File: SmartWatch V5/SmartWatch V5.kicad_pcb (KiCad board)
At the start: 4 copper layers, 23.7 x 34.2 mm, 61 parts, among them J1 10118192-0001LF, J10 TestPad, J2 , J8 TestPad, J9 TestPad, Q1 FDN340P, Q2 MMBT3904, Q3 MMBT3904, Q4 FDN028N20, Q5 FDN028N20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

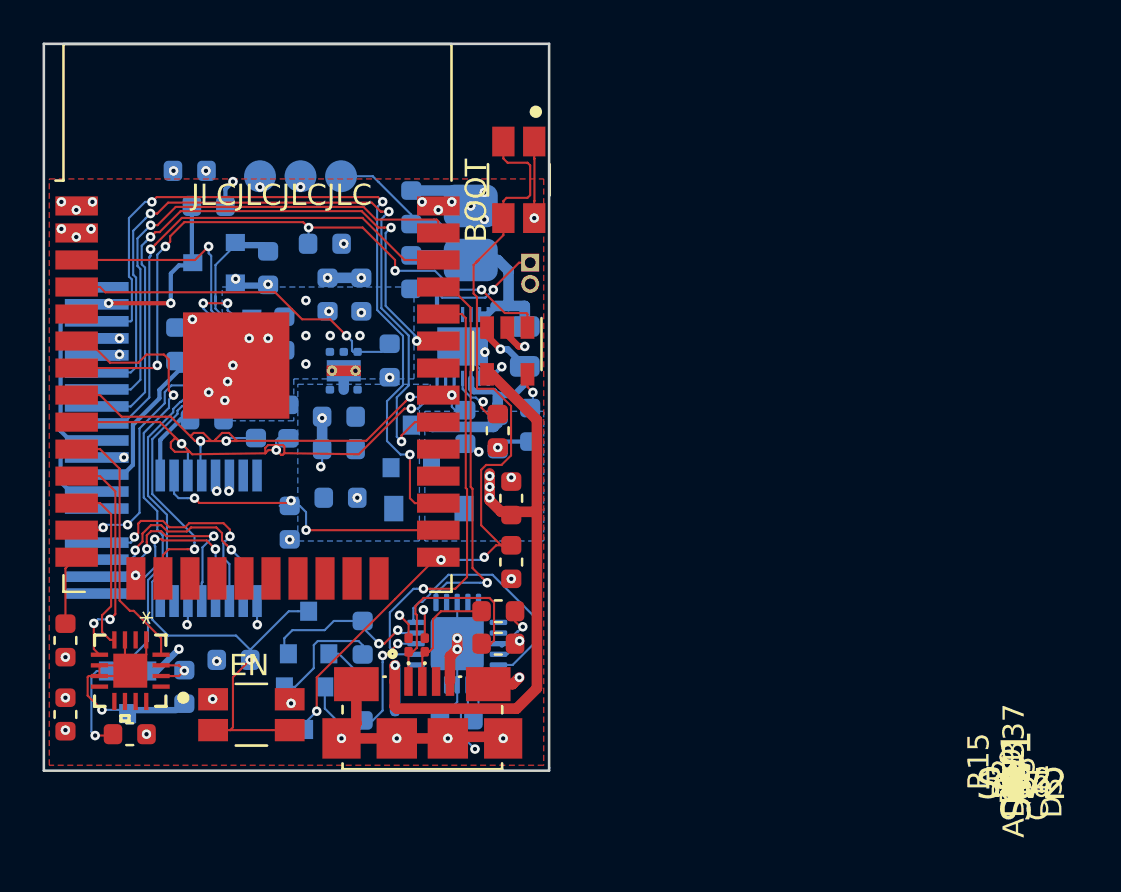
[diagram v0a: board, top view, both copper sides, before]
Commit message: Changed V5 schematic to remove enable mosfet from accelerometer
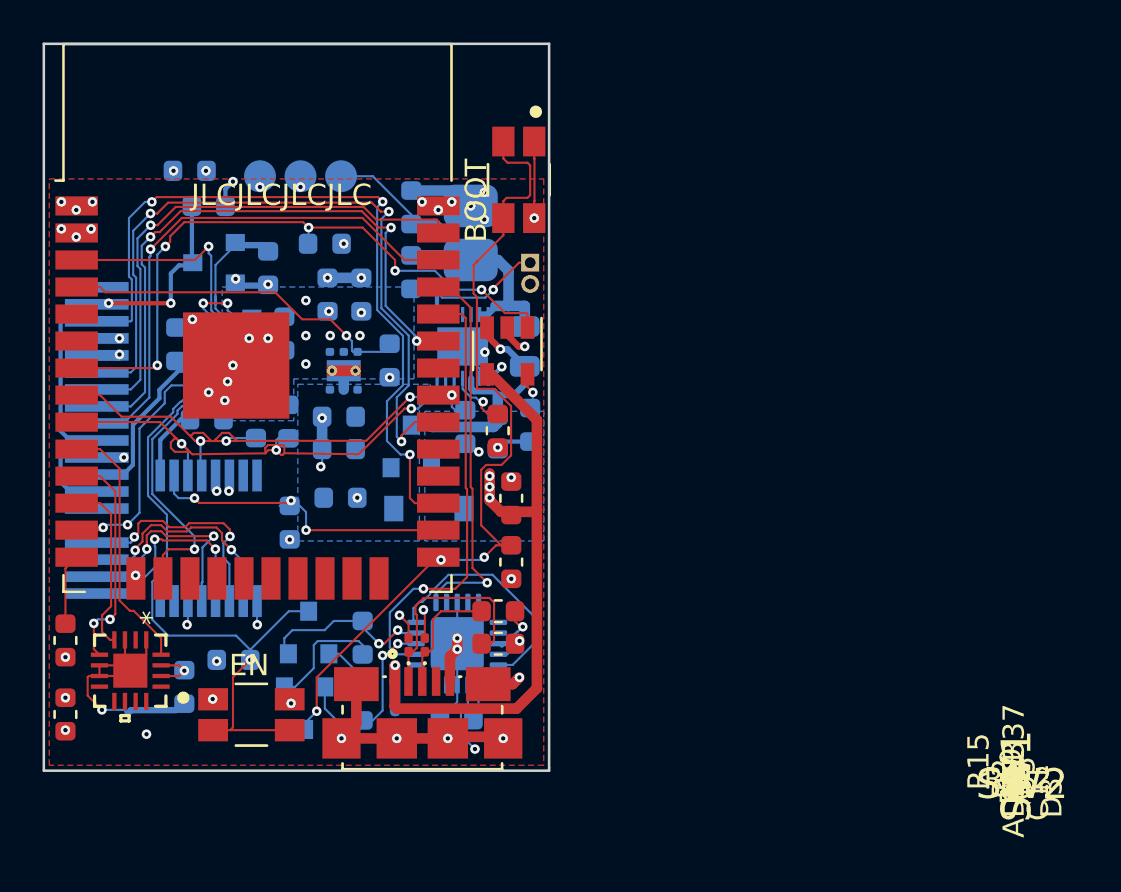
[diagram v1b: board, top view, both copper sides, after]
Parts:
- removed Q4: FDN028N20, Package_TO_SOT_SMD:SOT-23
- removed R20: 10k, Resistor_SMD:R_0603_1608Metric
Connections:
- C13 pad 2: /ACCEL_PWR -> GND
- U6 pad 6: /ACCEL_EN -> (no net)
- U8 pad 1: /ACCEL_PWR -> GND
- U8 pad 17: /ACCEL_PWR -> GND
- U8 pad 3: /ACCEL_PWR -> GND
- U8 pad 6: /ACCEL_PWR -> GND
- U8 pad 7: /ACCEL_PWR -> GND
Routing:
- net /ACCEL_EN: track 26.6 -> 0.00 mm, vias 2 -> 0
- net /ACCEL_PWR: track 12.6 -> 0.00 mm, vias 1 -> 0
- net GND: track 58.1 -> 68.8 mm
- net +3V3: track 12.1 -> 11.3 mm
